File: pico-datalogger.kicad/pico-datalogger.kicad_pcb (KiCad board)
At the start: 2 copper layers, 80 x 90 mm, 37 parts, among them J1 JST-PH2 VCC, J10 Conn_Inky_SW, J11 I2C_1, J12 I2C_7, J14 I2C_6, J16 BG_2, J18 I2C_5, J19 I2C_4, J2 I2C_8, J20 BG_3, J21 Conn_GND, J3 RFM9x_Lora_Breakout, J4 Alt-VCC, J5 Conn_I2S, J6 Conn_Inky_SPI, J7 Micro_SD_TF_PUSH, J8 Conn_ADC, J9 Conn_UART, SW1 SW_Push_SLIM, SW2 SW_Reset, U1 SN74HC74N, U2 PCF8523T, U3 Pico, Y1 Crystal

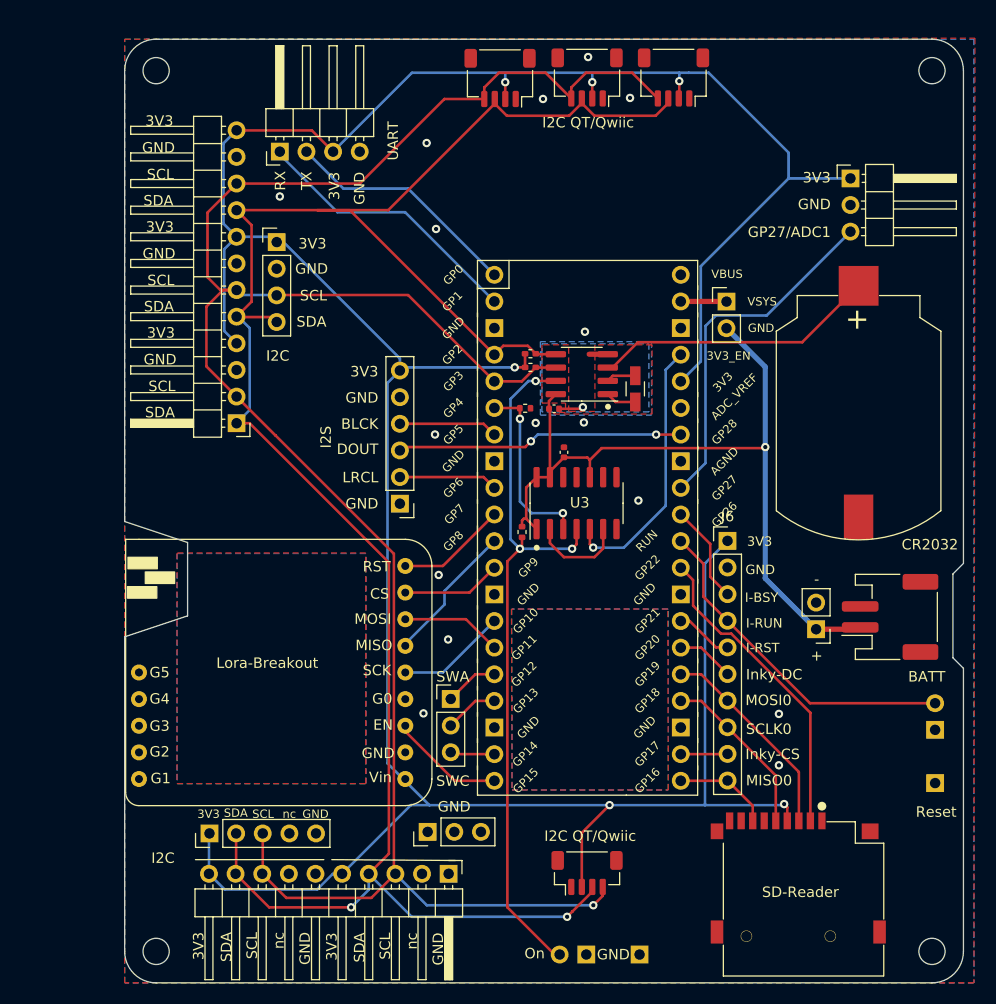
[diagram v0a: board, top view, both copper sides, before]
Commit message: Update pico-datalogger.kicad_pcb
- All pins are now on an inch/10 grid
- Added warning to disconnect jumper when using usb
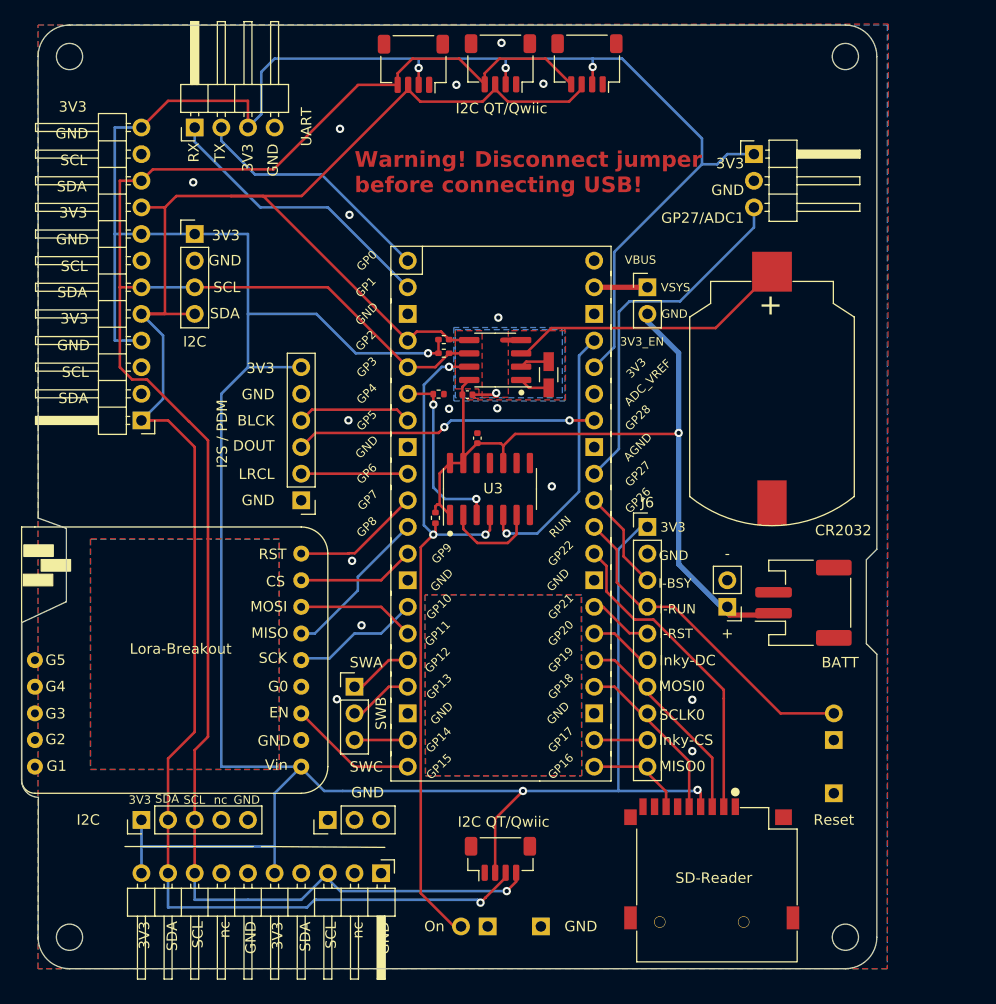
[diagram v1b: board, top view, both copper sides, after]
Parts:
- moved J3 9.99 mm to (116.8, 119.4)
- moved SW1 9.78 mm to (139.7, 134.6)
- moved SW2 9.71 mm to (167.6, 121.9)
- moved J21 9.59 mm to (119.4, 124.5)
- moved J8 9.49 mm to (160.0, 61.0)
- moved J5 9.42 mm to (116.8, 94.0)
- moved J10 9.25 mm to (121.9, 111.8)
- moved J11 9.08 mm to (101.6, 86.4)
- moved J4 8.73 mm to (157.5, 104.1)
- moved J9 8.44 mm to (106.7, 58.4)
- moved C1 8.37 mm to (133.6, 88.0)
- moved G*** 8.37 mm to (136.0, 65.0)
- moved R2 8.37 mm to (129.6, 95.7)
- moved U3 8.37 mm to (135.9, 95.2)
- moved H1 8.37 mm to (94.7, 51.6)
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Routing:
- net +3V3: track 299.2 -> 333.2 mm
- net /SDA: track 199.4 -> 193.8 mm, vias 2 -> 1
- net /SCL: track 202.7 -> 197.1 mm
- net /1~{PRE}: track 69.5 -> 67.7 mm
- net /BLCK: track 9.44 -> 11.0 mm
- net /DOUT: track 27.4 -> 29.0 mm
- net /MISO1: track 13.6 -> 15.1 mm
- net /Lora_RST: track 10.7 -> 12.3 mm
- net /Lora_CS: track 9.68 -> 11.2 mm
- net /SCLK1: track 10.7 -> 12.3 mm
- net /MOSI1: track 9.82 -> 11.2 mm
- net /Lora_EN: track 11.0 -> 12.3 mm
- net /TX: track 22.8 -> 23.8 mm
- net /Inky_SWA: track 5.14 -> 6.13 mm
- net /Inky_SWB: track 5.14 -> 6.13 mm
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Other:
- board size 80 x 90 mm -> 81.6 x 90 mm
- board text added: "I2S / PDM"
- board text added: "SWB"
- board text added: "Warning! Disconnect jumper before connecting USB!"
- board text removed: "I2S"
